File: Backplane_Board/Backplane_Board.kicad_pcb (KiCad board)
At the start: 4 copper layers, 179.7 x 127.9 mm, 188 parts, among them J10 Conn_01x02_Pin, J11 Conn_01x02_Pin, J12 Conn_01x02_Pin, J13 Conn_01x02_Pin, J14 Conn_01x02_Pin, J15 Conn_01x02_Pin, J16 Conn_01x02_Pin, J17 Conn_01x02_Pin, J18 Conn_01x02_Pin, J19 Conn_01x02_Pin, J20 Conn_01x02_Pin, J21 Conn_01x02_Pin, J22 Conn_01x02_Pin, J23 Conn_01x02_Pin, J24 Conn_01x02_Pin, J25 Conn_01x02_Pin, J26 Conn_01x02_Pin, J27 Conn_01x03_Pin, J28 Conn_01x03_Pin, J29 Conn_01x03_Pin, J3 Conn_01x02_Pin, J30 BM03B-SRSS-TB, J31 Conn_01x04, J32 Conn_01x05_Socket, J33 BM03B-SRSS-TB, J34 Connector_PinHeader_2.54mm:Pi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, J35 Connector_PinHeader_2.54mm:Pi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, J36 Conn_01x03_Pin, J37 Conn_01x02, J38 Conn_01x02, J39 Conn_01x02, J4 Conn_01x07_Female, J40 Conn_01x02, J41 Conn_01x02, J42 Conn_01x02, J44 Micro_SD_Card_Det2, J5 Conn_01x02_Pin, J6 Conn_01x02_Pin, J7 Conn_01x02_Pin, J8 Conn_01x02_Pin, J9 Conn_01x02_Pin, Q1 FDMS86163P, Q2 FDMS86163P, Q3 SI7615ADN-T1-GE3, Q4 ZXMN3A14F, Q5 ZXMN3A14F, Q6 ZXMN3A14F, Q7 ZXMN3A14F, Q8 ZXMN3A14F, Q9 ZXMN3A14F, SW1 SW_DPST_x2, U1 ZXTR2005ZQ-13, U2 PINA740AIREMR, U3 PKJ7213WPI, U4 PKJ7213WPI, U5 PKU3511SPI, U6 Pico

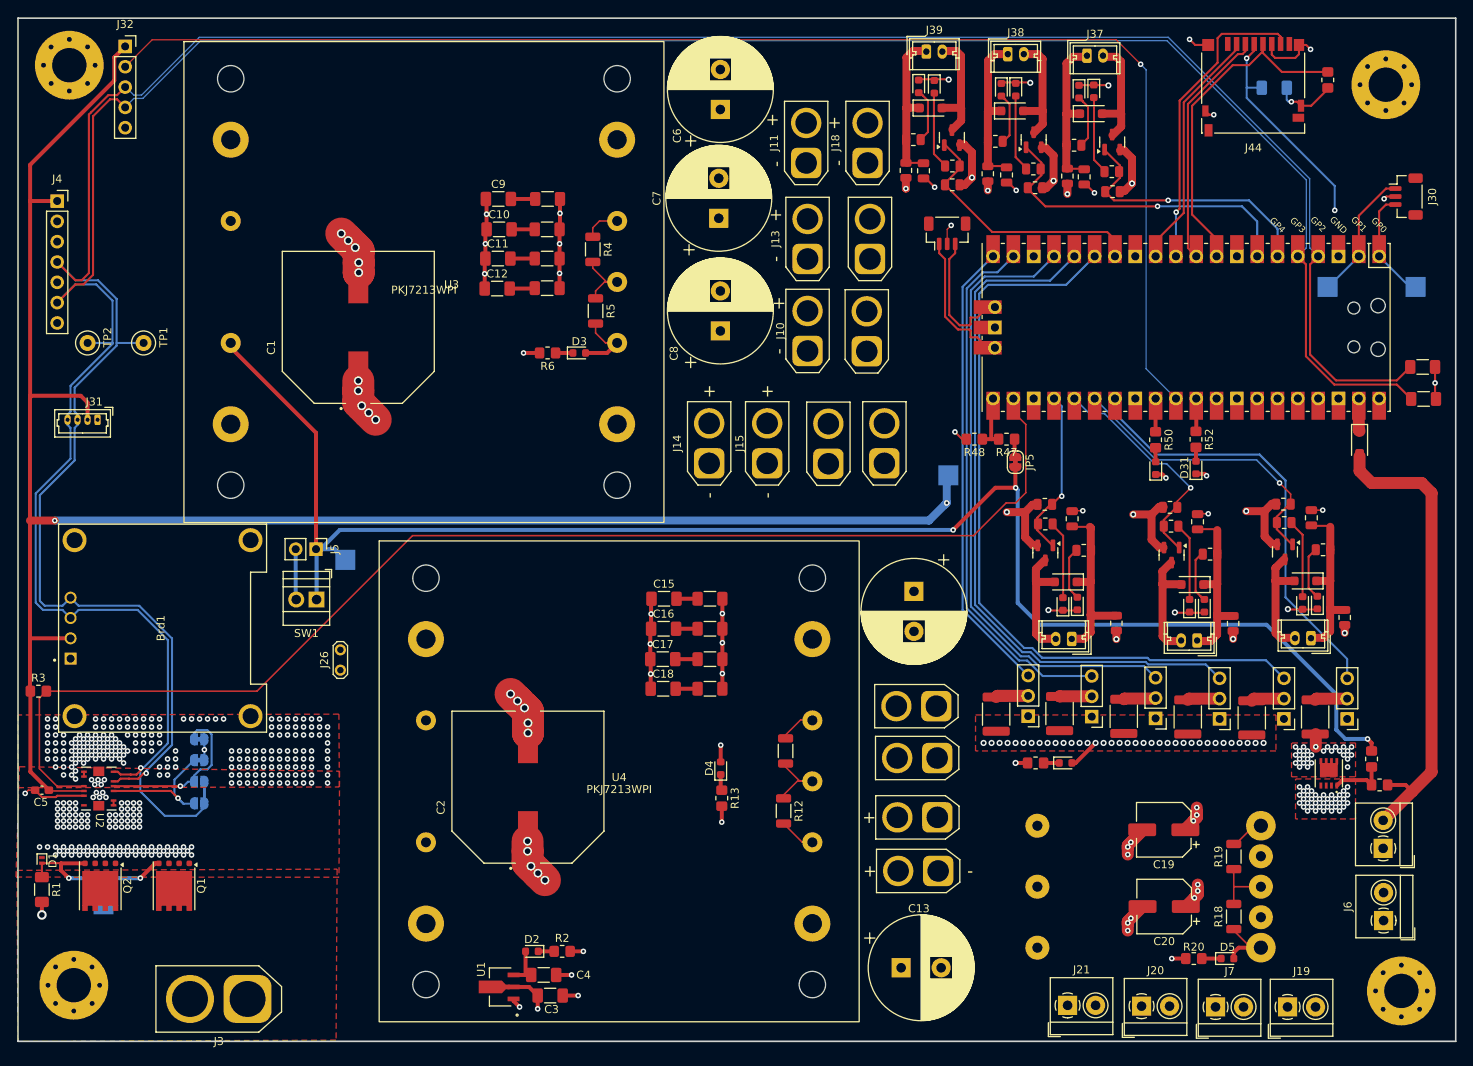
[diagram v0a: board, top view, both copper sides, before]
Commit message: killed more drc errors
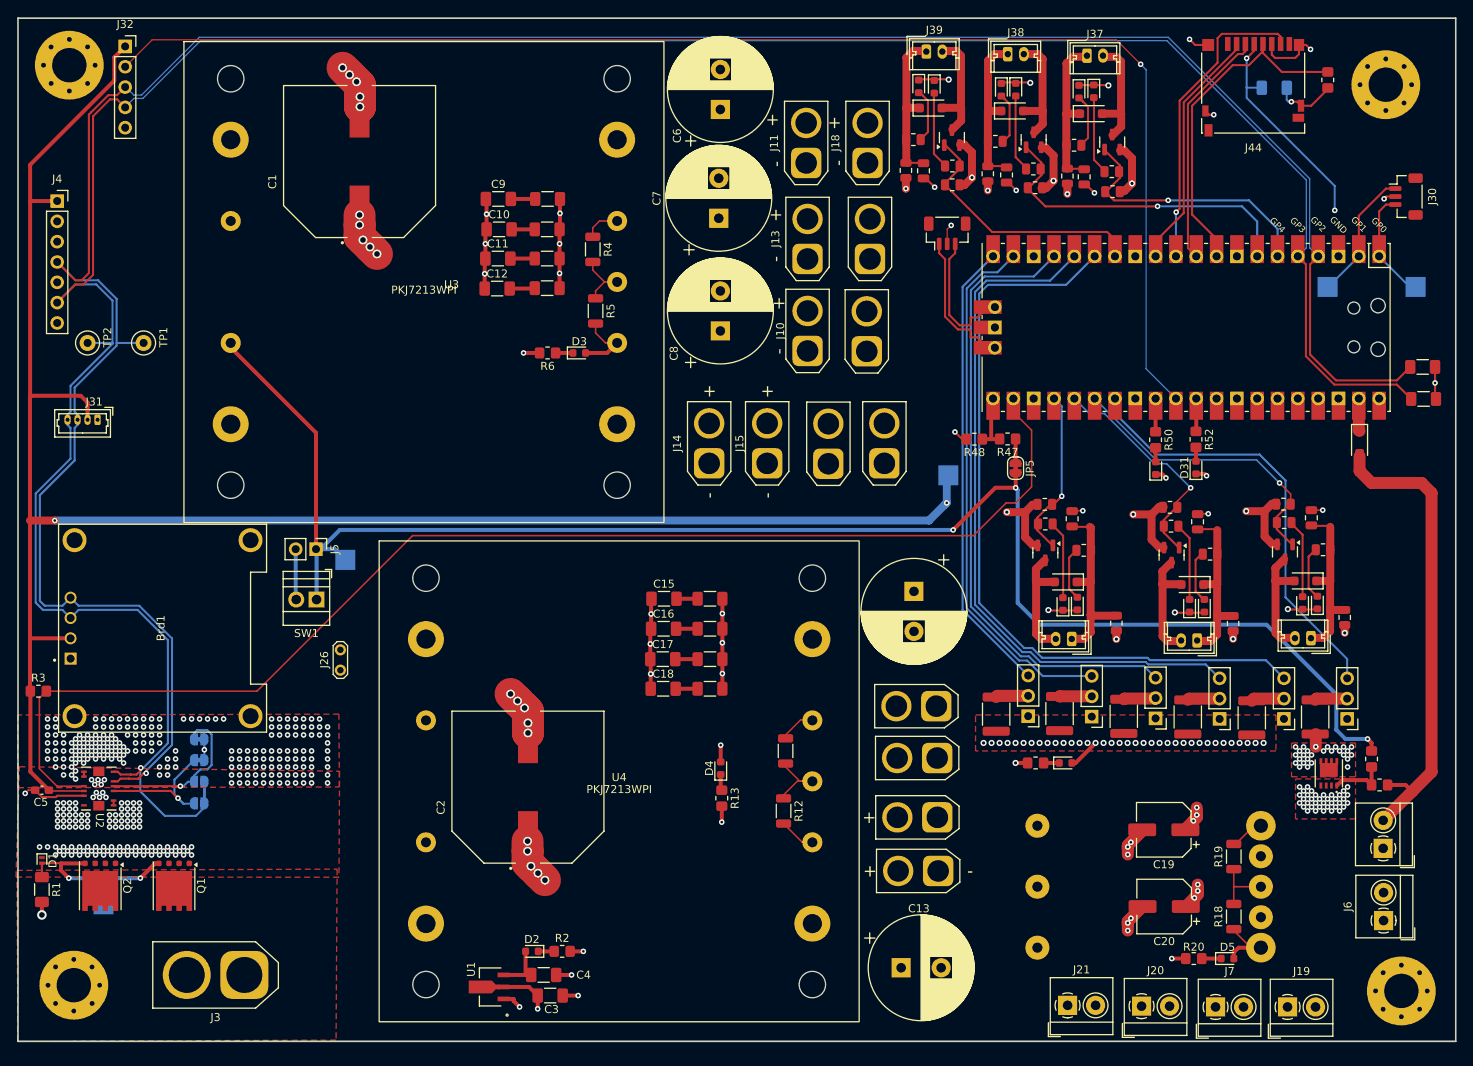
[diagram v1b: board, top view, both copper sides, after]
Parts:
- moved C1 20.7 mm to (74.0, 41.3)
- moved J3 3.03 mm to (59.6, 143.0)
- moved U1 1.25 mm to (90.3, 144.5)
- moved JP5 0.75 mm to (156.0, 79.7)
- moved R47 0.13 mm to (155.0, 76.0)
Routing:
- net Net-(U3-V_adj): track 8.62 -> 7.20 mm
- net Net-(D2-A): track 5.15 -> 6.40 mm
- net GND: track 195.0 -> 196.2 mm
- net 60V: track 16.7 -> 17.9 mm
- net Net-(JP5-A): track 2.27 -> 3.03 mm
- net KillSW: track 203.5 -> 202.8 mm
- net ALERT: track 161.6 -> 162.2 mm
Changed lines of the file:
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@@
 	(footprint "EEV-TG2A331M:CAP_EEVTG2A331M"
 		(layer "F.Cu")
-		(at 73.84 62.05 90)
+		(at 74 41.325 90)
 		(property "Reference" "C1"
 			(at -2.525 -10.885 90)
@@
 	(footprint "ZXTR2005ZQ-13:SOT-89_4P5X2P45_DIO-M"
 		(layer "F.Cu")
-		(at 91.5743 144.5 90)
+		(at 90.3236 144.5 90)
 		(tags "ZXTR2005ZQ-13 ")
 		(property "Reference" "U1"
@@
 	(footprint "Resistor_SMD:R_0805_2012Metric_Pad1.20x1.40mm_HandSolder"
 		(layer "F.Cu")
-		(at 154.875 76.025 180)
+		(at 155 76 180)
 		(descr "Resistor SMD 0805 (2012 Metric), square (rectangular) end terminal, IPC_7351 nominal with elongated pad for handsoldering. (Body size source: IPC-SM-782 page 72, https://www.pcb-3d.com/wordpress/wp-content/uploads/ipc-sm-782a_amendment_1_and_2.pdf), generated with kicad-footprint-generator")
 		(tags "resistor handsolder")
@@
 	(footprint "Connector_AMASS:AMASS_XT60-M_1x02_P7.20mm_Vertical"
 		(layer "F.Cu")
-		(at 60 146 180)
+		(at 59.6 143 180)
 		(descr "AMASS female XT60, through hole, vertical, https://www.tme.eu/Document/2d152ced3b7a446066e6c419d84bb460/XT60%20SPEC.pdf")
 		(tags "XT60 female vertical")
@@
 	(footprint "Jumper:SolderJumper-2_P1.3mm_Bridged_RoundedPad1.0x1.5mm"
 		(layer "F.Cu")
-		(at 155.975 78.9 -90)
+		(at 156 79.65 -90)
 		(descr "SMD Solder Jumper, 1x1.5mm, rounded Pads, 0.3mm gap, bridged with 1 copper strip")
 		(tags "net tie solder jumper bridged")
@@
 			(at 0 2.148 90)
 			(layer "B.SilkS")
+			(hide yes)
 			(effects
 				(font
@@
 			(at 0 -2.25 90)
 			(layer "B.Fab")
+			(hide yes)
 			(effects
 				(font
@@
 	)
 	(segment
-		(start 75.14 72.725)
-		(end 76.015 73.6)
-		(width 4)
-		(layer "F.Cu")
-		(net 1)
-	)
-	(segment
 		(start 95.1868 144.5)
-		(end 96.2618 145.575)
+		(end 92.0528 144.5)
 		(width 0.5)
 		(layer "F.Cu")
@@
 	)
 	(segment
-		(start 93.2507 144.5)
-		(end 95.1868 144.5)
-		(width 0.5)
+		(start 75.3 52)
+		(end 76.175 52.875)
+		(width 4)
 		(layer "F.Cu")
 		(net 1)
 	)
 	(segment
-		(start 73.84 71.425)
-		(end 74.265 71.85)
+		(start 74 50.7)
+		(end 74.425 51.125)
 		(width 4)
 		(layer "F.Cu")
@@
 	)
 	(segment
-		(start 73.84 69.975)
-		(end 73.84 71.425)
+		(start 74 49.25)
+		(end 74 50.7)
 		(width 4)
 		(layer "F.Cu")
@@
 	)
 	(segment
-		(start 73.84 68.725)
-		(end 73.84 69.975)
+		(start 96.2618 145.575)
+		(end 95.1868 144.5)
+		(width 0.5)
+		(layer "F.Cu")
+		(net 1)
+	)
+	(segment
+		(start 74 48)
+		(end 74 49.25)
 		(width 4)
 		(layer "F.Cu")
@@
 	)
 	(segment
-		(start 74.265 71.85)
-		(end 75.14 72.725)
+		(start 74.425 51.125)
+		(end 75.3 52)
 		(width 4)
 		(layer "F.Cu")
@@
 	)
 	(via
-		(at 76.015 73.6)
+		(at 76.175 52.875)
 		(size 1.1)
 		(drill 0.7)
@@
 	)
 	(via
-		(at 74.265 71.85)
+		(at 74.425 51.125)
 		(size 1.1)
 		(drill 0.7)
@@
 	)
 	(via
-		(at 75.14 72.725)
+		(at 75.3 52)
 		(size 1.1)
 		(drill 0.7)
@@
 	)
 	(via
-		(at 73.84 69.975)
+		(at 74 49.25)
 		(size 1.1)
 		(drill 0.7)
@@
 	)
 	(via
-		(at 73.84 68.725)
+		(at 74 48)
 		(size 1.1)
 		(drill 0.7)
@@
 	)
 	(segment
-		(start 73.89 55.225)
-		(end 73.89 55.2)
+		(start 74.05 34.5)
+		(end 74.05 34.475)
 		(width 4)
 		(layer "F.Cu")
@@
 	)
 	(segment
-		(start 72.59 51.2)
-		(end 71.715 50.325)
+		(start 72.75 30.475)
+		(end 71.875 29.6)
 		(width 4)
 		(layer "F.Cu")
@@
 	)
 	(segment
+		(start 93.2507 146)
+		(end 92 146)
+		(width 0.5)
+		(layer "F.Cu")
+		(net 2)
+	)
+	(segment
 		(start 179.6375 80.3625)
 		(end 179.875 80.6)
@@
 	)
 	(segment
-		(start 73.89 55.2)
-		(end 73.89 53.95)
+		(start 74.05 34.475)
+		(end 74.05 33.225)
 		(width 4)
 		(layer "F.Cu")
@@
 	)
 	(segment
-		(start 73.89 53.95)
-		(end 73.89 52.5)
+		(start 74.05 33.225)
+		(end 74.05 31.775)
 		(width 4)
 		(layer "F.Cu")
@@
 	)
 	(segment
-		(start 73.89 52.5)
-		(end 73.465 52.075)
+		(start 74.05 31.775)
+		(end 73.625 31.35)
 		(width 4)
 		(layer "F.Cu")
@@
 	)
 	(segment
-		(start 73.465 52.075)
-		(end 72.59 51.2)
+		(start 73.625 31.35)
+		(end 72.75 30.475)
 		(width 4)
 		(layer "F.Cu")
@@
 	)
 	(via
-		(at 73.89 53.95)
+		(at 74.05 33.225)
 		(size 1.1)
 		(drill 0.7)
@@
 	)
 	(via
-		(at 72.59 51.2)
+		(at 72.75 30.475)
 		(size 1.1)
 		(drill 0.7)
@@
 	)
 	(via
-		(at 73.465 52.075)
+		(at 73.625 31.35)
 		(size 1.1)
 		(drill 0.7)
@@
 	)
 	(via
-		(at 71.715 50.325)
+		(at 71.875 29.6)
 		(size 1.1)
 		(drill 0.7)
@@
 	)
 	(via
-		(at 73.89 55.2)
+		(at 74.05 34.475)
 		(size 1.1)
 		(drill 0.7)
@@
 	)
 	(segment
-		(start 93.2507 143)
-		(end 94.7493 143)
+		(start 94.7493 143)
+		(end 95.4493 143)
 		(width 0.5)
 		(layer "F.Cu")
@@
 	(segment
 		(start 94.7493 143)
-		(end 95.4493 143)
+		(end 92 143)
 		(width 0.5)
 		(layer "F.Cu")
@@
 	)
 	(segment
-		(start 155.975 79.55)
-		(end 155.975 82.058776)
+		(start 156.016224 82.1)
+		(end 156.016224 80.316224)
+		(width 0.5)
+		(layer "F.Cu")
+		(net 47)
+	)
+	(segment
+		(start 156.016224 80.316224)
+		(end 156 80.3)
 		(width 0.5)
 		(layer "F.Cu")
@@
 	)
 	(segment
-		(start 161.584925 83.16)
-		(end 160.569925 84.175)
+		(start 161.775 83.16)
+		(end 160.76 84.175)
 		(width 0.26)
 		(layer "F.Cu")
@@
 	)
 	(segment
-		(start 161.775 83.16)
-		(end 161.584925 83.16)
+		(start 160.4725 84.222425)
+		(end 160.336949 84.222425)
 		(width 0.26)
 		(layer "F.Cu")
@@
 	)
 	(segment
-		(start 160.4725 84.222425)
-		(end 160.336949 84.222425)
+		(start 160.76 84.175)
+		(end 160.569925 84.175)
 		(width 0.26)
 		(layer "F.Cu")
@@
 	)
 	(segment
-		(start 34.85 107.525)
-		(end 61.1818 107.525)
+		(start 150.74 88.085)
+		(end 154.825 84)
 		(width 0.2)
 		(layer "F.Cu")
@@
 	)
 	(segment
-		(start 155.725 72.63)
-		(end 155.725 70.95)
+		(start 80.6218 88.085)
+		(end 150.74 88.085)
 		(width 0.2)
 		(layer "F.Cu")
@@
 	)
 	(segment
-		(start 157.275 74.18)
-		(end 155.725 72.63)
+		(start 61.1818 107.525)
+		(end 80.6218 88.085)
 		(width 0.2)
 		(layer "F.Cu")
@@
 	)
 	(segment
-		(start 80.6218 88.085)
-		(end 150.74 88.085)
+		(start 156 84)
+		(end 158 82)
 		(width 0.2)
 		(layer "F.Cu")
@@
 	)
 	(segment
-		(start 156 84)
-		(end 157.275 82.725)
+		(start 33.975 117.2)
+		(end 33.975 108.4)
 		(width 0.2)
 		(layer "F.Cu")
@@
 	)
 	(segment
-		(start 61.1818 107.525)
-		(end 80.6218 88.085)
+		(start 155.725 72.63)
+		(end 155.725 70.95)
 		(width 0.2)
 		(layer "F.Cu")
@@
 	)
 	(segment
-		(start 33.975 117.2)
-		(end 33.975 108.4)
+		(start 33.975 108.4)
+		(end 34.85 107.525)
 		(width 0.2)
 		(layer "F.Cu")
@@
 	)
 	(segment
-		(start 33.975 108.4)
-		(end 34.85 107.525)
+		(start 36.175 119.4)
+		(end 33.975 117.2)
 		(width 0.2)
 		(layer "F.Cu")
@@
 	)
 	(segment
-		(start 36.175 119.4)
-		(end 33.975 117.2)
+		(start 34.85 107.525)
+		(end 61.1818 107.525)
 		(width 0.2)
 		(layer "F.Cu")
@@
 	)
 	(segment
-		(start 150.74 88.085)
-		(end 154.825 84)
+		(start 158 82)
+		(end 158 74.905)
 		(width 0.2)
 		(layer "F.Cu")
@@
 	)
 	(segment
-		(start 157.275 82.725)
-		(end 157.275 74.18)
+		(start 158 74.905)
+		(end 155.725 72.63)
 		(width 0.2)
 		(layer "F.Cu")
@@
 	)
 	(segment
-		(start 103.15 53.875)
-		(end 103.15 54.65)
-		(width 0.2)
-		(layer "F.Cu")
-		(net 62)
-	)
-	(segment
-		(start 104.875 56.375)
-		(end 106.195 56.375)
+		(start 103.15 54.9)
+		(end 104.625 56.375)
 		(width 0.2)
 		(layer "F.Cu")
@@
 	)
 	(segment
-		(start 103.15 54.65)
-		(end 104.875 56.375)
+		(start 103.15 53.875)
+		(end 103.15 54.9)
 		(width 0.2)
 		(layer "F.Cu")
@@
 	)
 	(segment
-		(start 155.875 78.15)
-		(end 155.975 78.25)
+		(start 156 76.15)
+		(end 155.875 76.025)
 		(width 0.5)
 		(layer "F.Cu")
@@
 	)
 	(segment
-		(start 155.875 76.025)
-		(end 155.875 78.15)
+		(start 156 79)
+		(end 156 76.15)
 		(width 0.5)
 		(layer "F.Cu")

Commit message: add 3d modules and clean up footprints
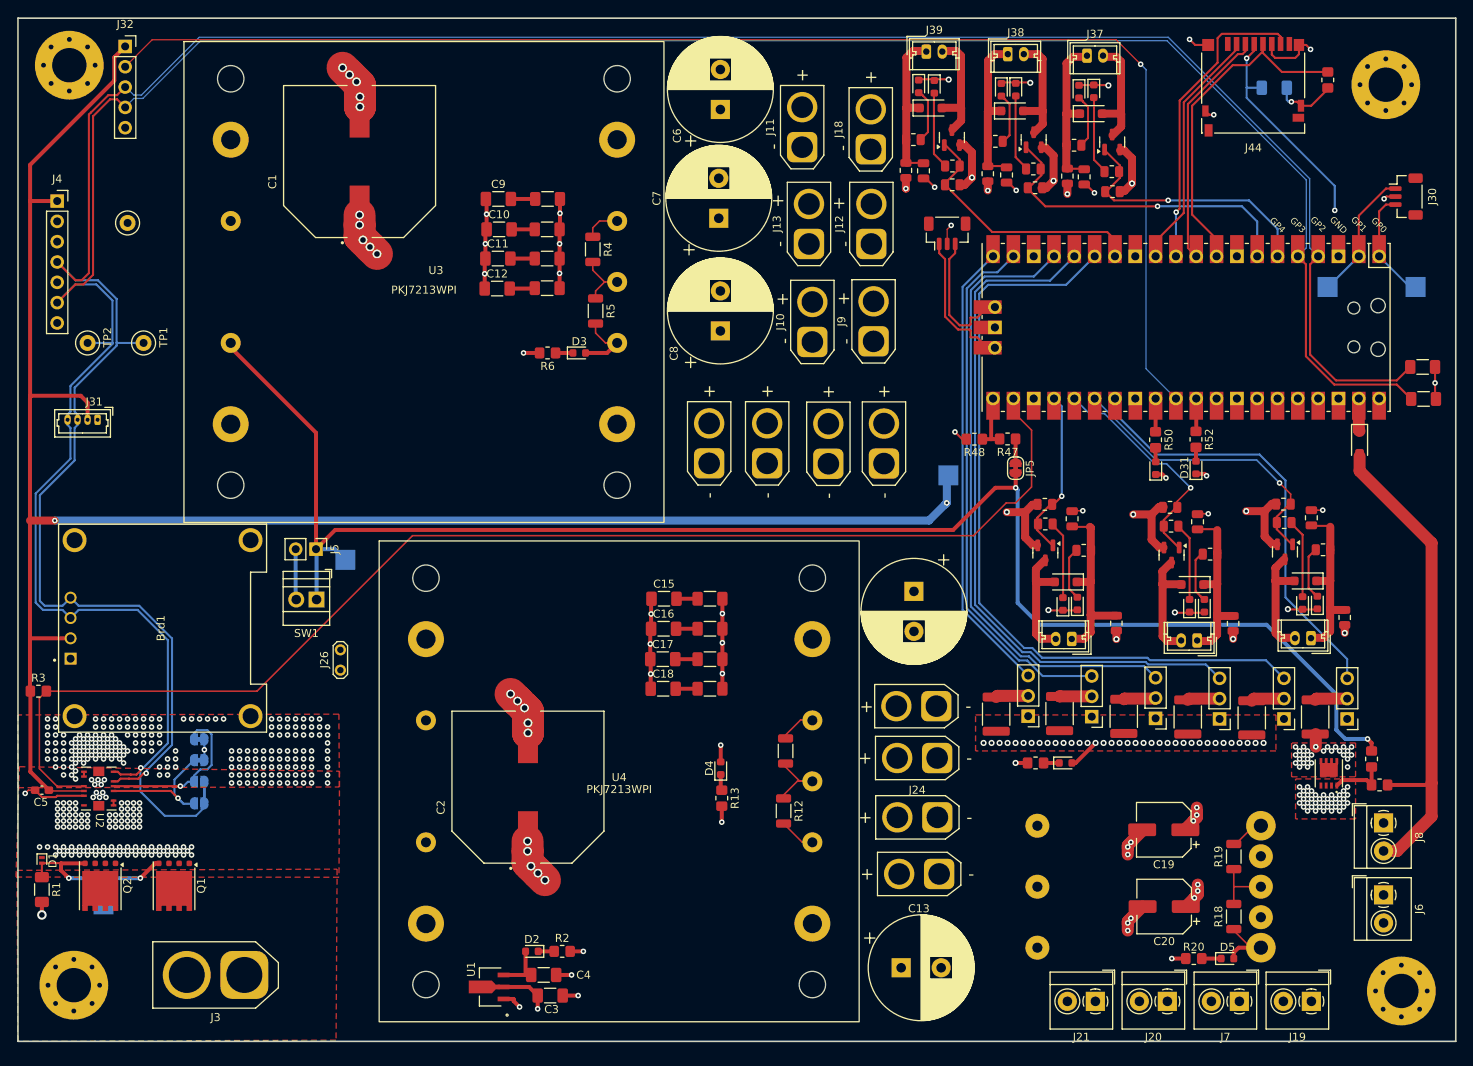
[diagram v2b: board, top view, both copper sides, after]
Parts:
- added TP8: TestPoint, TestPoint:TestPoint_Loop_D1.80mm_Drill1.0mm_Beaded, F.Cu at (45.0, 49.0)
- J10, J11, J12, J13, J14, J15, J16, J17, J18, J22, J23, J24, J25, J9: footprint Connector_AMASS:AMASS_XT30U-M_1x02_P5.0mm_Vertical -> XT30U-F_IW:AMASS_XT30U-M_1x02_P5.0mm_Vertical_IW_3d
- J19, J20, J21, J6, J7, J8: footprint TerminalBlock_4Ucon:TerminalBlock_4Ucon_1x02_P3.50mm_Horizontal -> 3.5_pitch_2x2_block:TerminalBlock_4Ucon_1x02_P3.50mm_Horizontal_updated
- moved J21 3.51 mm to (166.0, 146.3), turned to 180 degrees
- moved J20 3.28 mm to (175.0, 146.3), turned to 180 degrees
- moved J6 3.20 mm to (202.0, 133.0), turned to -90 degrees
- moved J8 3.18 mm to (202.0, 124.0), turned to -90 degrees
- moved J19 3.06 mm to (193.0, 146.3), turned to 180 degrees
- moved J7 3.06 mm to (184.0, 146.3), turned to 180 degrees
- moved J11 2.04 mm to (129.3, 39.5)
- moved J13 1.88 mm to (130.2, 51.6)
- moved J12 1.88 mm to (138.0, 51.6)
- moved J18 1.75 mm to (137.9, 39.8)
- moved J9 1.51 mm to (138.2, 63.8)
- moved J10 1.27 mm to (130.6, 63.9)
- moved J22 0.40 mm to (146.4, 130.4)
- moved J17 0.06 mm to (139.6, 79.1)
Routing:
- net +5V: track 74.4 -> 77.7 mm
- net KillSW: track 202.8 -> 203.4 mm, vias 3 -> 2

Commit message: add anotations
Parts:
- moved TP8 31.5 mm to (46.2, 80.4)
- moved J26 3.15 mm to (69.2, 107.0), turned to 180 degrees
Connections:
- J3 pad 1: PWR_IN -> GND
- J3 pad 2: GND -> PWR_IN
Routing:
- net 60V: track 17.9 -> 19.4 mm, vias 217 -> 211
- net GND: track 196.2 -> 196.5 mm, vias 60 -> 54
- net SHUNT+: vias 112 -> 200
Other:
- board text added: "+"
- board text added: "12V Clean Power On"
- board text added: "12V ESC Power"
- board text added: "3V3"
- board text added: "5V Clean Power"
- board text added: "5V Kill Switch Power"
- board text added: "BME 280"
- board text added: "Damping"
- board text added: "GND"
- board text added: "I2C 3V3 Pullup"
- board text added: "Input Power"
- board text added: "Kill Switch"
- board text added: "KillSW Status"
- board text added: "LaserShark Backplane Board REV1 Designed by Isaac Wax 2024"
- board text added: "OLED"
- board text added: "Power In (14 - 160V)"
- board text added: "RC"
- board text added: "RUN"
- board text added: "RX"
- board text added: "SCL"
- board text added: "SDA"
- board text added: "SPI 0"
- board text added: "SWCLK"
- board text added: "SWDIO"
- board text added: "TX"
- board text added: "V_in TP"
- board text added: "github.com/CabrilloRoboticsClub/robosub_electrical"

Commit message: added gerber
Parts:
- R13, R6: value 2k -> 10k
- R2, R20, R24: value 620 -> 1k
- R34, R35, R36, R41, R44, R45: value 10k -> 2k
- U1: footprint ZXTR2005ZQ-13:SOT-89_4P5X2P45_DIO-M -> Package_TO_SOT_SMD:SOT-89-3_Handsoldering
- moved TP1 2.68 mm to (44.3, 64.1)
- moved U1 0.65 mm to (89.7, 144.6), turned to 180 degrees
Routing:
- net I2C-: track 340.9 -> 324.2 mm
- net I2C+: track 324.0 -> 313.8 mm
- net Net-(D2-A): track 6.40 -> 7.01 mm
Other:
- rule pad_to_mask_clearance: 0.0508 -> 0
- board text added: "Input Power Status"
- board text added: "Rx"
- board text added: "Tx"
- board text removed: "Input Power"
